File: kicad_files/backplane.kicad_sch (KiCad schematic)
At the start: 60 parts, among them J10 5051101592, Q7 TEMT6000X01, SW4 SW_SPDT, SW5 SW_SPDT, U11 MCP3427-xUN, U12 BQ25570

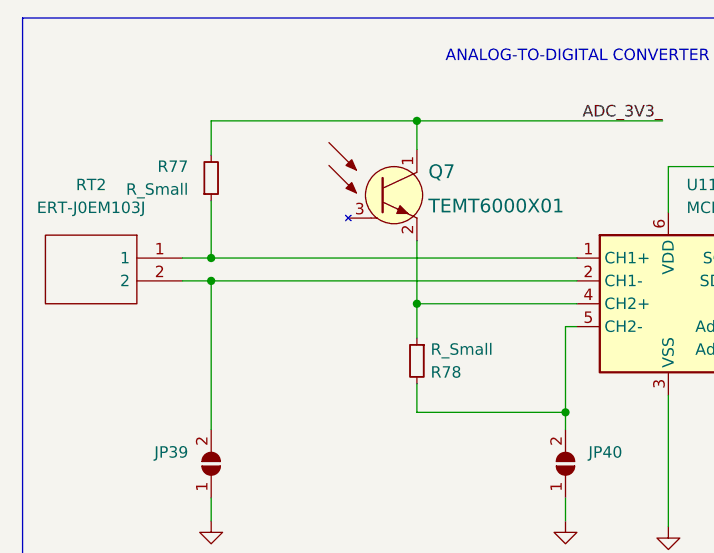
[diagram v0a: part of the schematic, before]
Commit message: update components values
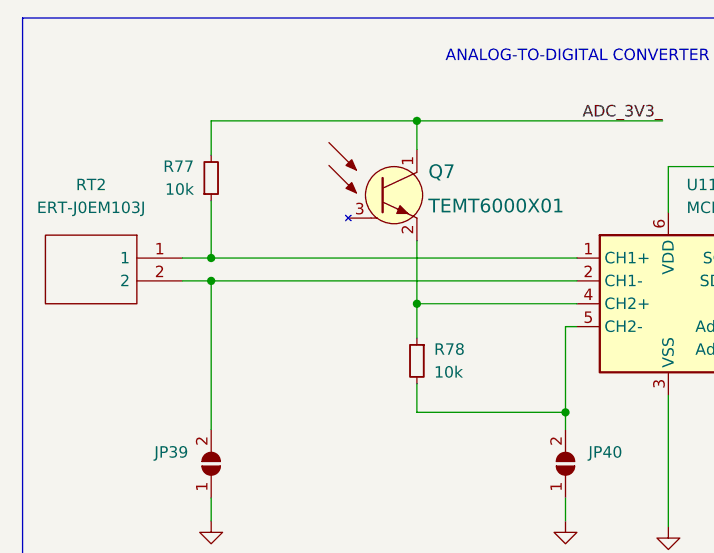
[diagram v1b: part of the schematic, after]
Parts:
- R77, R78: value R_Small -> 10k
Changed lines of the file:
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@@
   (symbol (lib_id "Device:R_Small") (at 57.785 62.23 0) (mirror y) (unit 1)
     (in_bom yes) (on_board yes) (fields_autoplaced)
-    (property "Reference" "R78" (id 0) (at 59.309 63.5001 0)
-      (effects (font (size 1.27 1.27)) (justify right))
-    )
-    (property "Value" "R_Small" (id 1) (at 59.309 60.9601 0)
+    (property "Reference" "R78" (id 0) (at 59.69 60.9599 0)
+      (effects (font (size 1.27 1.27)) (justify right))
+    )
+    (property "Value" "10k" (id 1) (at 59.69 63.4999 0)
       (effects (font (size 1.27 1.27)) (justify right))
     )
@@
   (symbol (lib_id "Device:R_Small") (at 34.925 41.91 0) (mirror x) (unit 1)
     (in_bom yes) (on_board yes) (fields_autoplaced)
-    (property "Reference" "R77" (id 0) (at 32.385 40.6399 0)
-      (effects (font (size 1.27 1.27)) (justify right))
-    )
-    (property "Value" "R_Small" (id 1) (at 32.385 43.1799 0)
-      (effects (font (size 1.27 1.27)) (justify right))
-    )
+    (property "Reference" "R77" (id 0) (at 33.02 40.6399 0)
+      (effects (font (size 1.27 1.27)) (justify right))
+    )
+    (property "Value" "10k" (id 1) (at 33.02 43.1799 0)
+      (effects (font (size 1.27 1.27)) (justify right))
+    )
